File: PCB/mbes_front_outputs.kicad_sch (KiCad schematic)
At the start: 55 parts, among them IC2 BDX34C, IC3 BDX34C, Q1 D45VH10, Q10 BC337, Q14 D45VH10, Q15 D45VH10, Q2 D45VH10, Q3 BC337, Q4 BC337, Q5 BC337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

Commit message: Merged files
These files have been merged by remotes/origin/ATmega16__dualPCB__bluetoothCockpit branch
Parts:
- removed IC2, IC3: BDX34C, BDX34C:TO270P460X1020X2008-3P, symbol BDX34C:BDX34C
- removed Q1, Q14, Q15, Q2: D45VH10, Package_TO_SOT_THT:TO-220-3_Vertical, symbol D45VH10:D45VH10
- removed Q10, Q3, Q4, Q5, Q6, Q7, Q8, Q9: BC337, Package_TO_SOT_THT:TO-92L_Inline_Wide, symbol Transistor_BJT:BC337
- added Q1, Q14, Q15, Q19, Q2, Q20, Q21, Q3: BC817, Package_TO_SOT_SMD:SOT-23, symbol Transistor_BJT:BC817
- added Q4, Q5, Q6, Q7, Q8, Q9: IRF4905, Package_TO_SOT_THT:TO-220-3_Vertical, symbol Transistor_FET:IRF4905
- RA1, RA2, RA3, RA4, RA5, RA6, RA9: footprint Resistor_THT:R_Axial_DIN0207_L6.3mm_D2.5mm_P10.16mm_Horizontal -> Resistor_SMD:R_1206_3216Metric
- RA10, RA11, RA12: footprint Resistor_THT:R_Axial_DIN0414_L11.9mm_D4.5mm_P15.24mm_Horizontal -> Resistor_SMD:R_1206_3216Metric
- RA13, RA14, RA16, RA17, RA18, RA19, RA20, RA21, RA22, RA24, RA25, RA26, RA27, RA28, RA32, RA34, RA35, RA36, RA37, RA38, RA39, RA40, RA7: footprint Resistor_THT:R_Axial_DIN0207_L6.3mm_D2.5mm_P7.62mm_Horizontal -> Resistor_SMD:R_1206_3216Metric
- RA15: value 240 -> 8K; footprint Resistor_THT:R_Axial_DIN0414_L11.9mm_D4.5mm_P15.24mm_Horizontal -> Resistor_SMD:R_1206_3216Metric
- RA42: value 100K -> 8K; footprint Resistor_THT:R_Axial_DIN0207_L6.3mm_D2.5mm_P7.62mm_Horizontal -> Resistor_SMD:R_1206_3216Metric
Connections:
- net +12V: now also RA42.2; no longer RA42.1
- net GND: now also Q1.2 (E), Q14.2 (E), Q15.2 (E), Q19.2 (E), Q2.2 (E), Q20.2 (E), Q21.2 (E), Q3.2 (E)
- net c_leftArrow: now also Q15.3 (C); no longer RA27.2
- net c_rightArrow: now also Q19.3 (C); no longer RA28.2
- net at RA15.1: now also RA42.1, Q9.1 (G)
- net at RA15.2: now also Q3.3 (C); no longer RA42.2
- net at RA1.1, RA10.1: now also Q1.3 (C); no longer RA24.2
- net at RA32.1, RA7.1: now also Q3.1 (B)
- net at RA10.2: now also RA24.2, Q4.1 (G)
- net at addLight_p1.1 (Pin_1): now also Q4.3 (S)
- net at addLight_p1.2 (Pin_2): now also Q4.2 (D)
- net at RA12.1, RA3.1: now also Q14.3 (C); no longer RA26.2
- net at RA6.1: now also Q20.3 (C)
- net at RA17.1, RA39.1: now also Q20.1 (B)
- net at RA20.1, RA36.1: now also Q14.1 (B)
- net at RA13.2: now also RA27.2, Q7.1 (G)
- net at RA22.1, RA34.1: now also Q1.1 (B)
- net at RA19.1, RA37.1: now also Q15.1 (B)
- net at RA11.1, RA2.1: now also Q2.3 (C); no longer RA25.2
- net at RA21.1, RA35.1: now also Q2.1 (B)
- net at DownLight_p1.1 (Pin_1): now also Q6.3 (S)
- net at DownLight_p1.2 (Pin_2): now also Q6.2 (D)
- net at Horn_p1.1 (Pin_1): now also Q9.3 (S)
- net at Horn_p1.2 (Pin_2): now also Q9.2 (D)
- net at RA11.2: now also RA25.2, Q5.1 (G)
- net at UpLight_p1.1 (Pin_1): now also Q5.3 (S)
- net at UpLight_p1.2 (Pin_2): now also Q5.2 (D)
- net at RA14.2: now also RA28.2, Q8.1 (G)
- net at Arrow_p1.3 (Pin_3): now also Q8.2 (D)
- net at Arrow_p1.2 (Pin_2): now also Q7.3 (S), Q8.3 (S)
- net at RA18.1, RA38.1: now also Q19.1 (B)
- net at RA9.1: now also Q21.3 (C)
- net at RA16.1, RA40.1: now also Q21.1 (B)
- net at Arrow_p1.1 (Pin_1): now also Q7.2 (D)
- net at RA12.2: now also RA26.2, Q6.1 (G)
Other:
- moved on the sheet: Arrow_p1, DownLight_p1, Horn_p1, UpLight_p1, addLight_p1

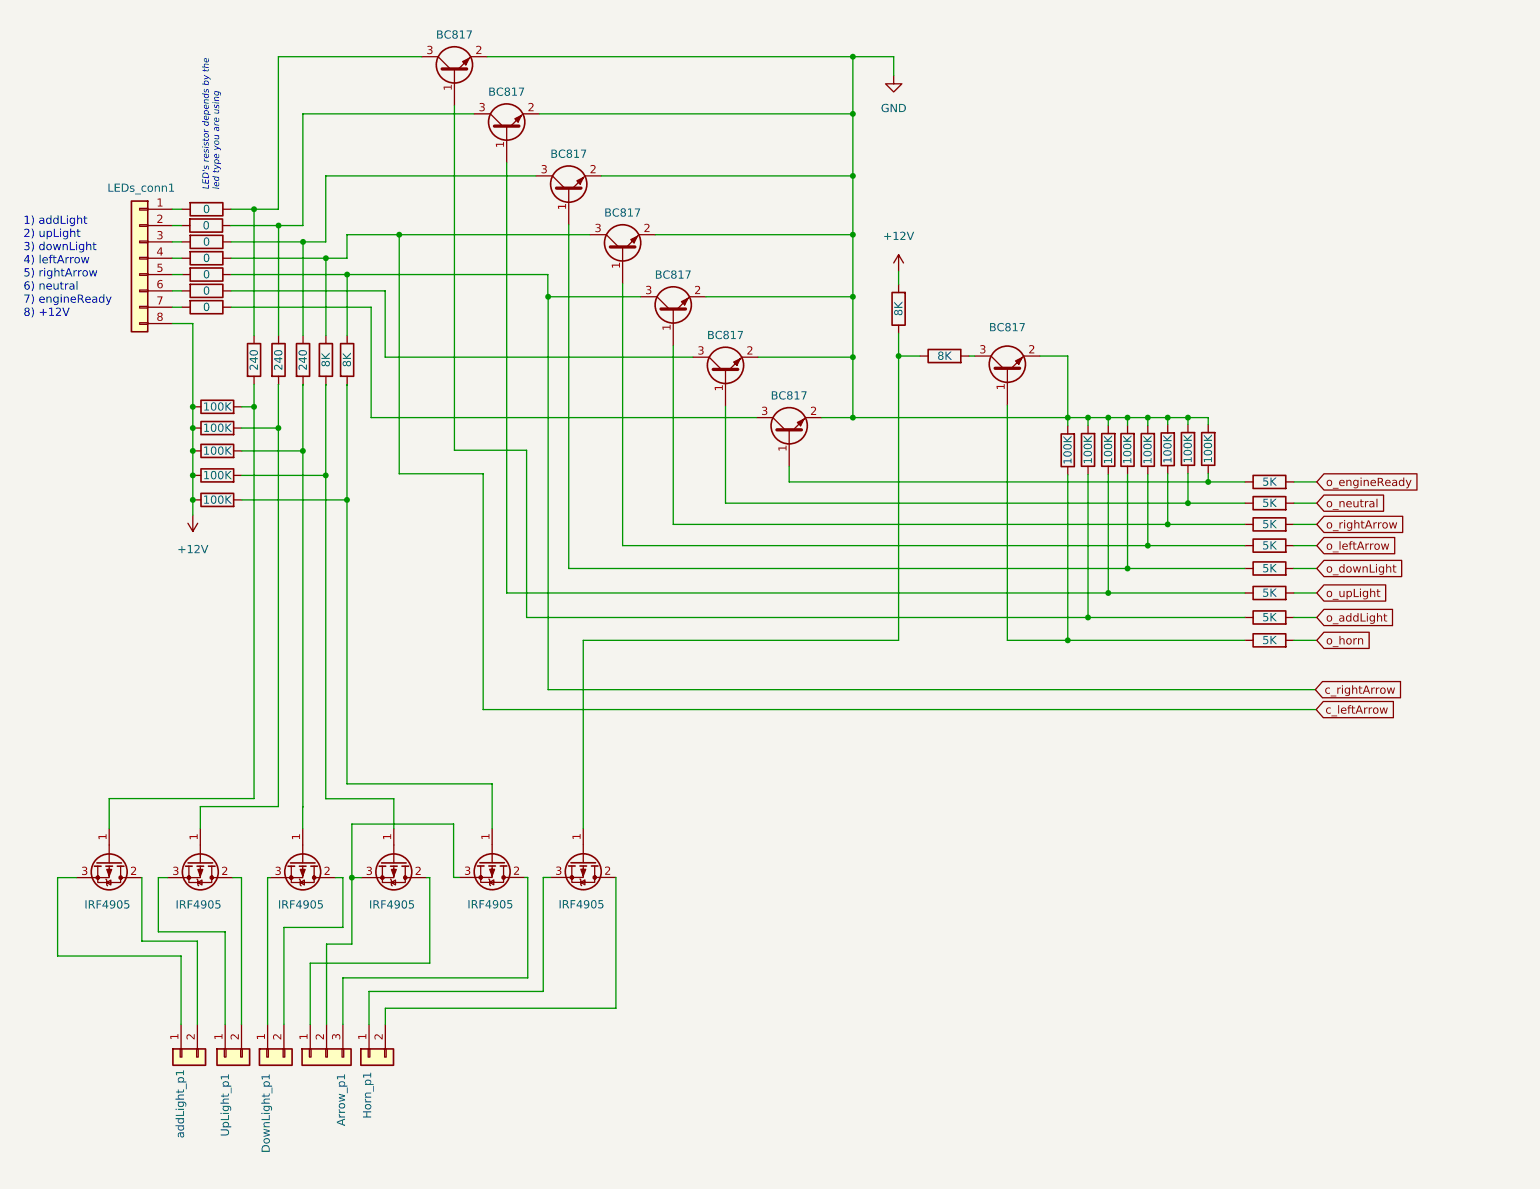
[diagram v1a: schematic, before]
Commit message: SMD version using TPCA8120
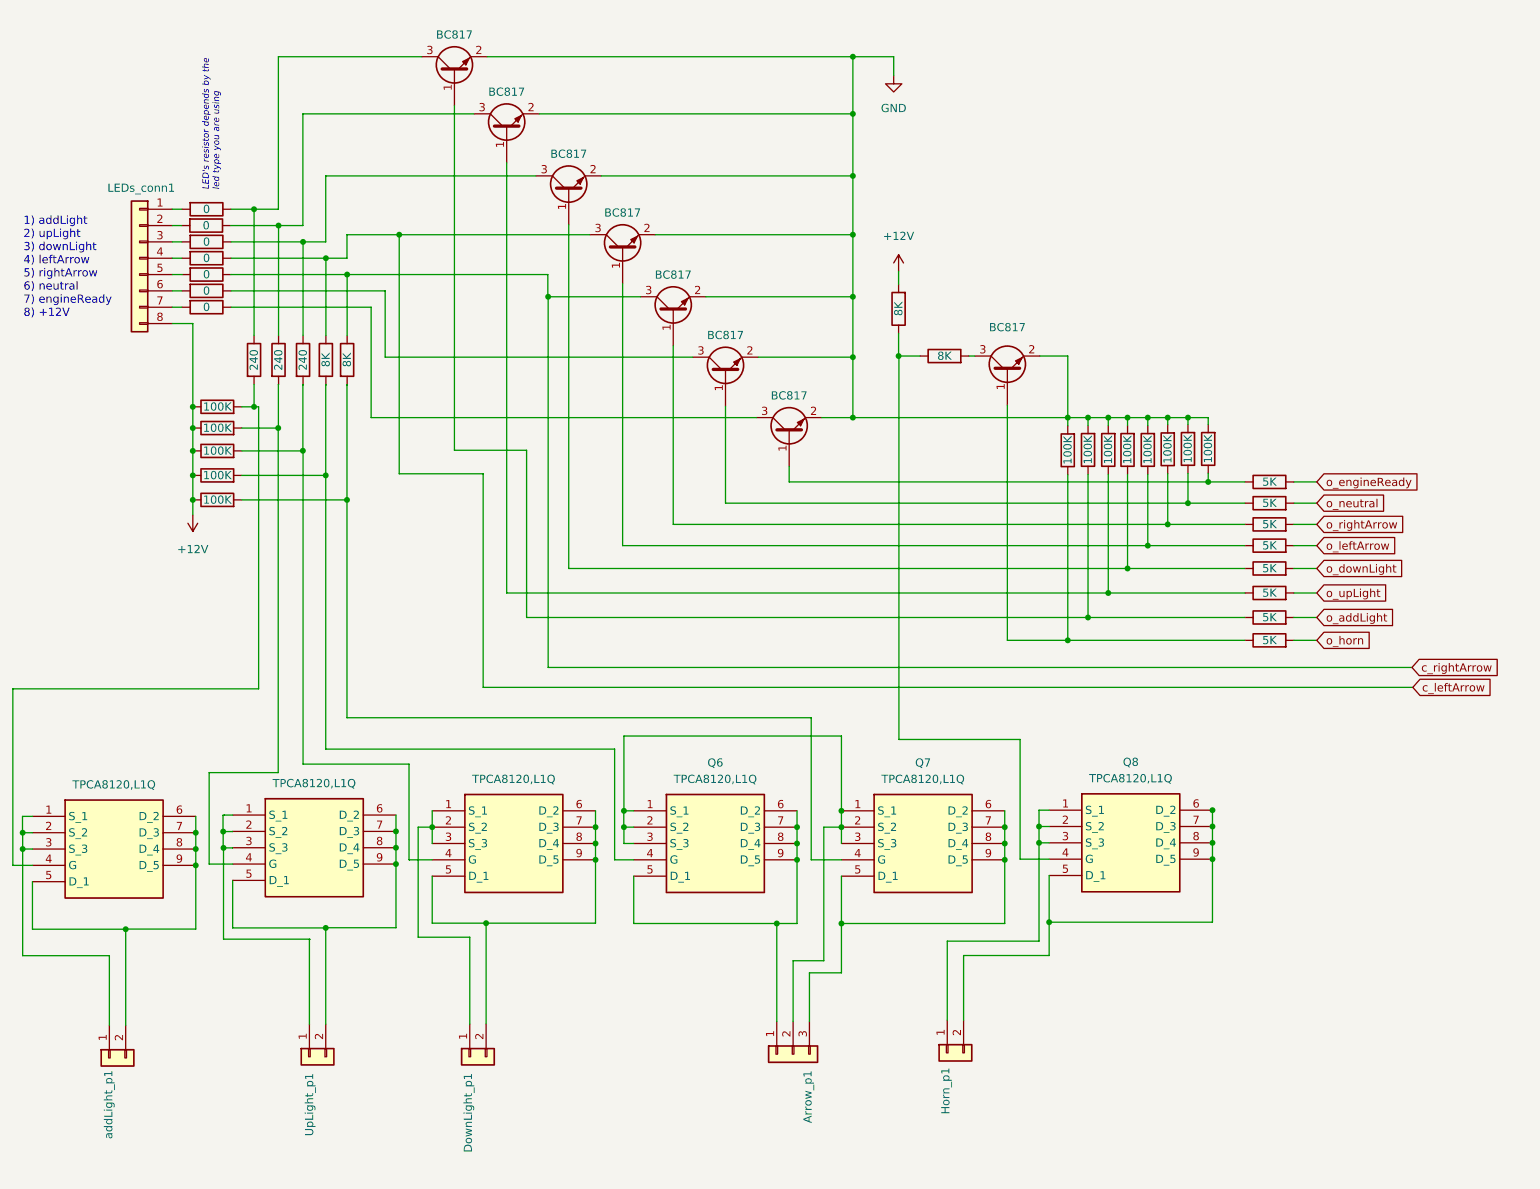
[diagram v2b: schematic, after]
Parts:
- removed Q4, Q5, Q6, Q7, Q8, Q9: IRF4905, Package_TO_SOT_THT:TO-220-3_Vertical, symbol Transistor_FET:IRF4905
- added Q11, Q4, Q5, Q6, Q7, Q8: TPCA8120,L1Q, TPCA8120:SOP Advance_TOS-L, symbol TPCA8120-LQ:TPCA8120,L1Q
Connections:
- net at RA10.2, RA24.2: now also Q11.4 (G)
- net at RA12.2, RA26.2: now also Q5.4 (G)
- net at RA14.2, RA28.2: now also Q7.4 (G)
- net at Arrow_p1.3 (Pin_3): now also Q7.5 (D_1), Q7.6 (D_2), Q7.7 (D_3), Q7.8 (D_4), Q7.9 (D_5)
- net at Arrow_p1.2 (Pin_2): now also Q6.1 (S_1), Q6.2 (S_2), Q6.3 (S_3), Q7.1 (S_1), Q7.2 (S_2), Q7.3 (S_3)
- net at RA13.2, RA27.2: now also Q6.4 (G)
- net at Arrow_p1.1 (Pin_1): now also Q6.5 (D_1), Q6.6 (D_2), Q6.7 (D_3), Q6.8 (D_4), Q6.9 (D_5)
- net at RA11.2, RA25.2: now also Q4.4 (G)
- net at UpLight_p1.2 (Pin_2): now also Q4.5 (D_1), Q4.6 (D_2), Q4.7 (D_3), Q4.8 (D_4), Q4.9 (D_5)
- net at UpLight_p1.1 (Pin_1): now also Q4.1 (S_1), Q4.2 (S_2), Q4.3 (S_3)
- net at DownLight_p1.1 (Pin_1): now also Q5.1 (S_1), Q5.2 (S_2), Q5.3 (S_3)
- net at DownLight_p1.2 (Pin_2): now also Q5.5 (D_1), Q5.6 (D_2), Q5.7 (D_3), Q5.8 (D_4), Q5.9 (D_5)
- net at Horn_p1.1 (Pin_1): now also Q8.1 (S_1), Q8.2 (S_2), Q8.3 (S_3)
- net at Horn_p1.2 (Pin_2): now also Q8.5 (D_1), Q8.6 (D_2), Q8.7 (D_3), Q8.8 (D_4), Q8.9 (D_5)
- net at RA15.1, RA42.1: now also Q8.4 (G)
- net at addLight_p1.1 (Pin_1): now also Q11.1 (S_1), Q11.2 (S_2), Q11.3 (S_3)
- net at addLight_p1.2 (Pin_2): now also Q11.5 (D_1), Q11.6 (D_2), Q11.7 (D_3), Q11.8 (D_4), Q11.9 (D_5)
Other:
- moved on the sheet: Arrow_p1, DownLight_p1, Horn_p1, UpLight_p1, addLight_p1

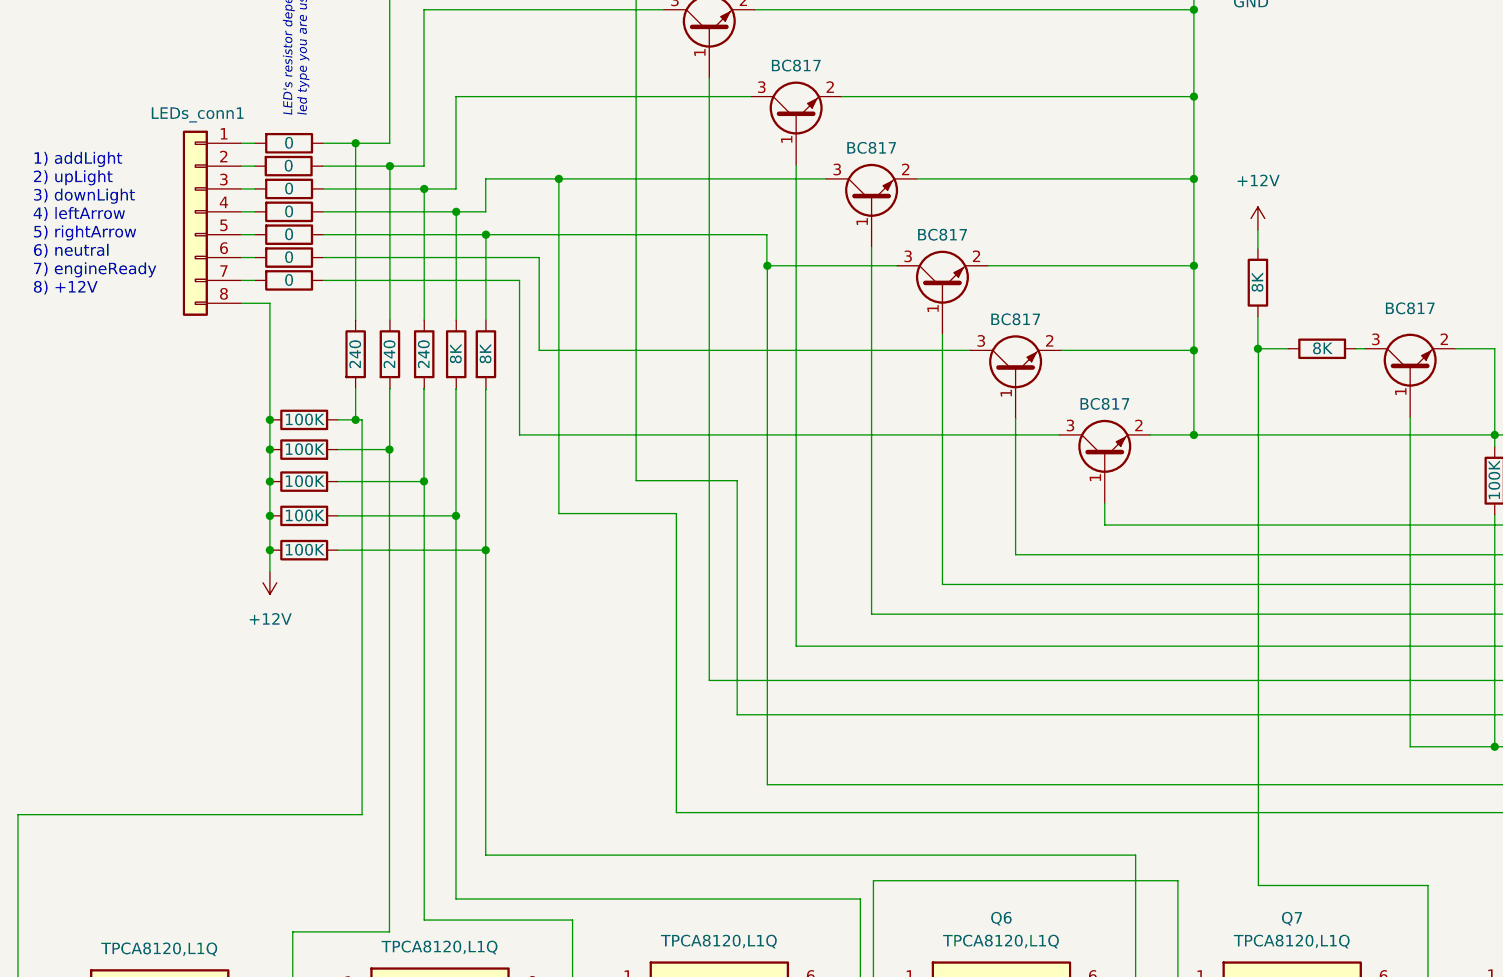
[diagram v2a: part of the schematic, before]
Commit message: Many changes
- The power drivers component has been implemented with TPCA8120 P-ch MOSfet
- The temp-power management has been moved from pcb-a to pcb-b
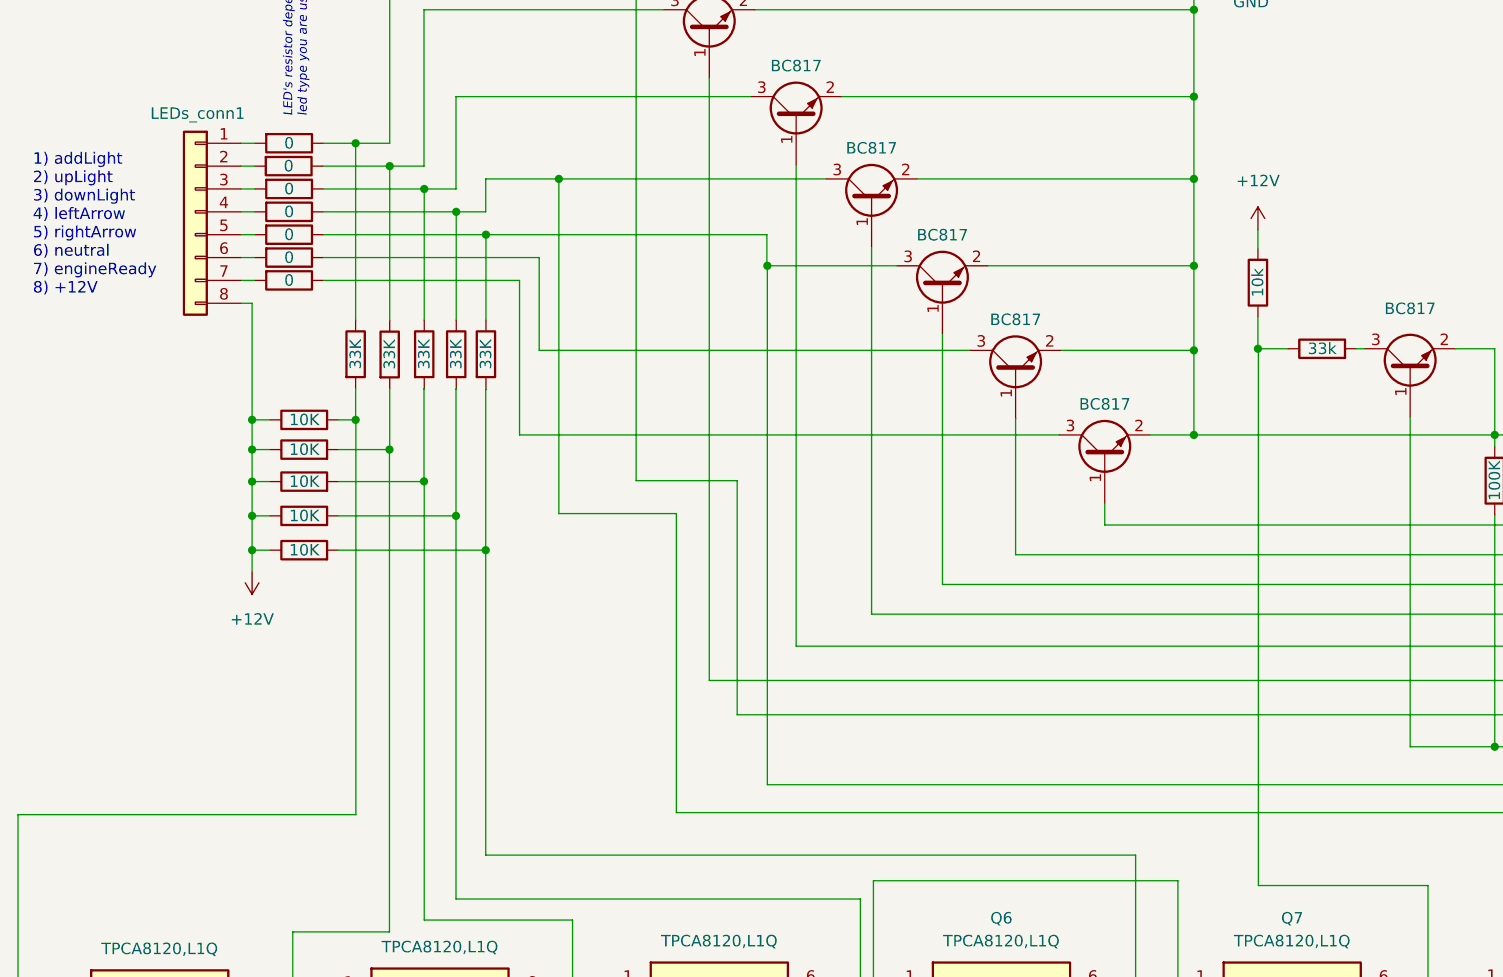
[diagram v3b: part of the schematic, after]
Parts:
- Q11, Q4, Q5, Q6, Q7, Q8: footprint TPCA8120:SOP Advance_TOS-L -> TPCA8120:TPH4R003NLL1Q
- RA10, RA11, RA12: value 240 -> 33K
- RA13, RA14: value 8K -> 33K
- RA15: value 8K -> 33k
- RA24, RA25, RA26, RA27, RA28: value 100K -> 10K
- RA42: value 8K -> 10k

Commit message: Manual merging from the ATmega16__dualPCB branch
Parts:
- removed Q20, Q3: BC817, Package_TO_SOT_SMD:SOT-23, symbol Transistor_BJT:BC817
- removed RA15: 33k, Resistor_SMD:R_1206_3216Metric, symbol Device:R
- removed RA17: 5K, Resistor_SMD:R_1206_3216Metric, symbol Device:R
- removed RA32, RA39: 100K, Resistor_SMD:R_1206_3216Metric, symbol Device:R
- added engReadyLed1: Conn_01x02, Connector_PinHeader_2.54mm:PinHeader_1x02_P2.54mm_Vertical, symbol Connector_Generic:Conn_01x02
- LEDs_conn1: footprint Connector_PinHeader_2.54mm:PinHeader_1x08_P2.54mm_Vertical -> Connector_PinHeader_2.54mm:PinHeader_2x04_P2.54mm_Vertical
- RA42: value 10k -> 10K
- RA7: value 5K -> 33K
- RA9: value 0 -> 1K
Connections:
- net +12V: now also RA9.2
- net at RA7.1: now also Q8.4 (G), RA42.1
- net at Q21.3 (C): now also engReadyLed1.2 (Pin_2); no longer RA9.1
- net at LEDs_conn1.7 (Pin_7): no longer RA9.2
- net c_neutral: now reaches RA6.1
- net o_horn renamed c_horn
- new net: RA9.1, engReadyLed1.1 (Pin_1)
- no-connect marks 0 -> 1
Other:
- note added: "1) addLight 2) upLight 3) downLight 4) leftArrow 5) rightArrow 6) neutral 7) NC 8) +12V"
- note removed: "1) addLight 2) upLight 3) downLight 4) leftArrow 5) rightArrow 6) neutral 7) engineReady 8) +12V"
- moved on the sheet: LEDs_conn1

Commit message: Old files replaced.
They have been merged for error
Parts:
- removed engReadyLed1: Conn_01x02, Connector_PinHeader_2.54mm:PinHeader_1x02_P2.54mm_Vertical, symbol Connector_Generic:Conn_01x02
- added Q20, Q3: BC817, Package_TO_SOT_SMD:SOT-23, symbol Transistor_BJT:BC817
- added RA15: 33k, Resistor_SMD:R_1206_3216Metric, symbol Device:R
- added RA17: 5K, Resistor_SMD:R_1206_3216Metric, symbol Device:R
- added RA32, RA39: 100K, Resistor_SMD:R_1206_3216Metric, symbol Device:R
- LEDs_conn1: footprint Connector_PinHeader_2.54mm:PinHeader_2x04_P2.54mm_Vertical -> Connector_PinHeader_2.54mm:PinHeader_1x08_P2.54mm_Vertical
- RA42: value 10K -> 10k
- RA7: value 33K -> 5K
- RA9: value 1K -> 0
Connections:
- net +12V: no longer RA9.2
- net GND: now also Q20.2 (E), Q3.2 (E), RA32.2, RA39.2
- net at Q21.3 (C): now also RA9.1
- net at LEDs_conn1.7 (Pin_7): now also RA9.2
- net at Q8.4 (G), RA42.1: now also RA15.1; no longer RA7.1
- net c_horn renamed o_horn
- net c_neutral: no longer names the net of RA6.1
- net c_neutral: now also Q20.3 (C)
- new net: Q3.1 (B), RA32.1, RA7.1
- new net: Q3.3 (C), RA15.2
- new net: Q20.1 (B), RA17.1, RA39.1
- new net o_neutral: RA17.2
- no-connect marks 1 -> 0
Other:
- note added: "1) addLight 2) upLight 3) downLight 4) leftArrow 5) rightArrow 6) neutral 7) engineReady 8) +12V"
- note removed: "1) addLight 2) upLight 3) downLight 4) leftArrow 5) rightArrow 6) neutral 7) NC 8) +12V"
- moved on the sheet: LEDs_conn1
